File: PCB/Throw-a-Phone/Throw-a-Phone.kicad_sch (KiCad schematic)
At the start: 30 parts, among them J1 GSM Module Left, J2 GSM Module Right, J3 Conn_01x04_Pin, SW1 SW_Push, SW10 SW_Push, SW11 SW_Push, SW12 SW_Push, SW2 SW_Push, SW3 SW_Push, SW4 SW_Push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

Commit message: Made PCB, fixed design
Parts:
- J1, J2: footprint (none) -> Connector_PinHeader_2.00mm:PinHeader_1x07_P2.00mm_Vertical
- J3: footprint (none) -> footprints:SSD1306-0.91-OLED-4pin-128x32
- LS1, MK1: footprint (none) -> Connector_PinHeader_2.00mm:PinHeader_1x02_P2.00mm_Vertical
- SW1, SW10, SW11, SW12, SW2, SW3, SW4, SW5, SW6, SW7, SW8, SW9: footprint (none) -> Button_Switch_THT:SW_PUSH_6mm_H5mm
- U1: footprint ESP32-C3_SUPERMINI_TH:MODULE_ESP32-C3_SUPERMINI_TH -> footprints:MODULE_ESP32-C3_SUPERMINI_TH
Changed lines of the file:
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@@
 			)
 		)
-		(property "Footprint" "ESP32-C3_SUPERMINI_TH:MODULE_ESP32-C3_SUPERMINI_TH"
+		(property "Footprint" "footprints:MODULE_ESP32-C3_SUPERMINI_TH"
 			(at 163.83 102.87 0)
 			(effects
@@
 			)
 		)
-		(property "Footprint" ""
+		(property "Footprint" "Button_Switch_THT:SW_PUSH_6mm_H5mm"
 			(at 81.28 147.32 0)
 			(effects
@@
 			)
 		)
-		(property "Footprint" ""
+		(property "Footprint" "Button_Switch_THT:SW_PUSH_6mm_H5mm"
 			(at 55.88 71.12 0)
 			(effects
@@
 			)
 		)
-		(property "Footprint" ""
+		(property "Footprint" "Button_Switch_THT:SW_PUSH_6mm_H5mm"
 			(at 106.68 96.52 0)
 			(effects
@@
 			)
 		)
-		(property "Footprint" ""
+		(property "Footprint" "Button_Switch_THT:SW_PUSH_6mm_H5mm"
 			(at 81.28 96.52 0)
 			(effects
@@
 			)
 		)
-		(property "Footprint" ""
+		(property "Footprint" "Connector_PinHeader_2.00mm:PinHeader_1x02_P2.00mm_Vertical"
 			(at 255.27 120.65 0)
 			(effects
@@
 			)
 		)
-		(property "Footprint" ""
+		(property "Footprint" "Button_Switch_THT:SW_PUSH_6mm_H5mm"
 			(at 55.88 96.52 0)
 			(effects
@@
 			)
 		)
-		(property "Footprint" ""
+		(property "Footprint" "Button_Switch_THT:SW_PUSH_6mm_H5mm"
 			(at 55.88 147.32 0)
 			(effects
@@
 			)
 		)
-		(property "Footprint" ""
+		(property "Footprint" "Connector_PinHeader_2.00mm:PinHeader_1x02_P2.00mm_Vertical"
 			(at 226.06 118.11 90)
 			(effects
@@
 			)
 		)
-		(property "Footprint" ""
+		(property "Footprint" "Button_Switch_THT:SW_PUSH_6mm_H5mm"
 			(at 81.28 71.12 0)
 			(effects
@@
 			)
 		)
-		(property "Footprint" ""
+		(property "Footprint" "Button_Switch_THT:SW_PUSH_6mm_H5mm"
 			(at 81.28 121.92 0)
 			(effects
@@
 			)
 		)
-		(property "Footprint" ""
+		(property "Footprint" "Connector_PinHeader_2.00mm:PinHeader_1x07_P2.00mm_Vertical"
 			(at 243.84 87.63 0)
 			(effects
@@
 			)
 		)
-		(property "Footprint" ""
+		(property "Footprint" "Button_Switch_THT:SW_PUSH_6mm_H5mm"
 			(at 106.68 121.92 0)
 			(effects
@@
 			)
 		)
-		(property "Footprint" ""
+		(property "Footprint" "Button_Switch_THT:SW_PUSH_6mm_H5mm"
 			(at 106.68 71.12 0)
 			(effects
@@
 			)
 		)
-		(property "Footprint" ""
+		(property "Footprint" "Button_Switch_THT:SW_PUSH_6mm_H5mm"
 			(at 55.88 121.92 0)
 			(effects
@@
 			)
 		)
-		(property "Footprint" ""
+		(property "Footprint" "Connector_PinHeader_2.00mm:PinHeader_1x07_P2.00mm_Vertical"
 			(at 228.6 90.17 0)
 			(effects
@@
 			)
 		)
-		(property "Footprint" ""
+		(property "Footprint" "Button_Switch_THT:SW_PUSH_6mm_H5mm"
 			(at 106.68 147.32 0)
 			(effects
@@
 			)
 		)
-		(property "Footprint" ""
+		(property "Footprint" "footprints:SSD1306-0.91-OLED-4pin-128x32"
 			(at 158.75 53.34 0)
 			(effects

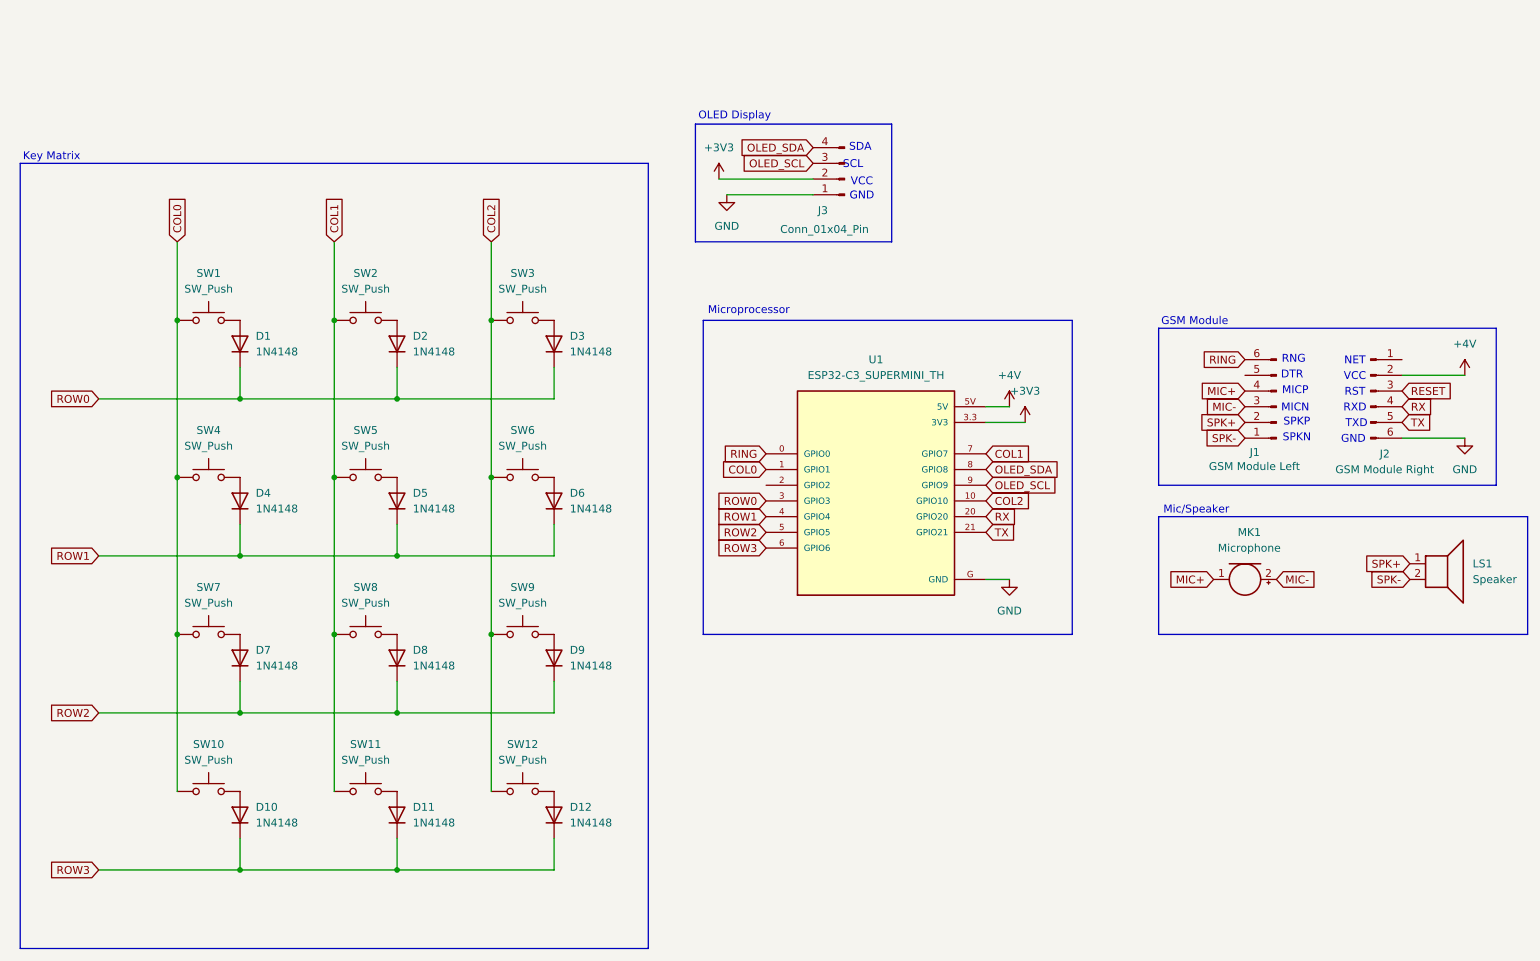
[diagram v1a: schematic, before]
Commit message: Updated readme, added images. Fixed PCB edge cuts
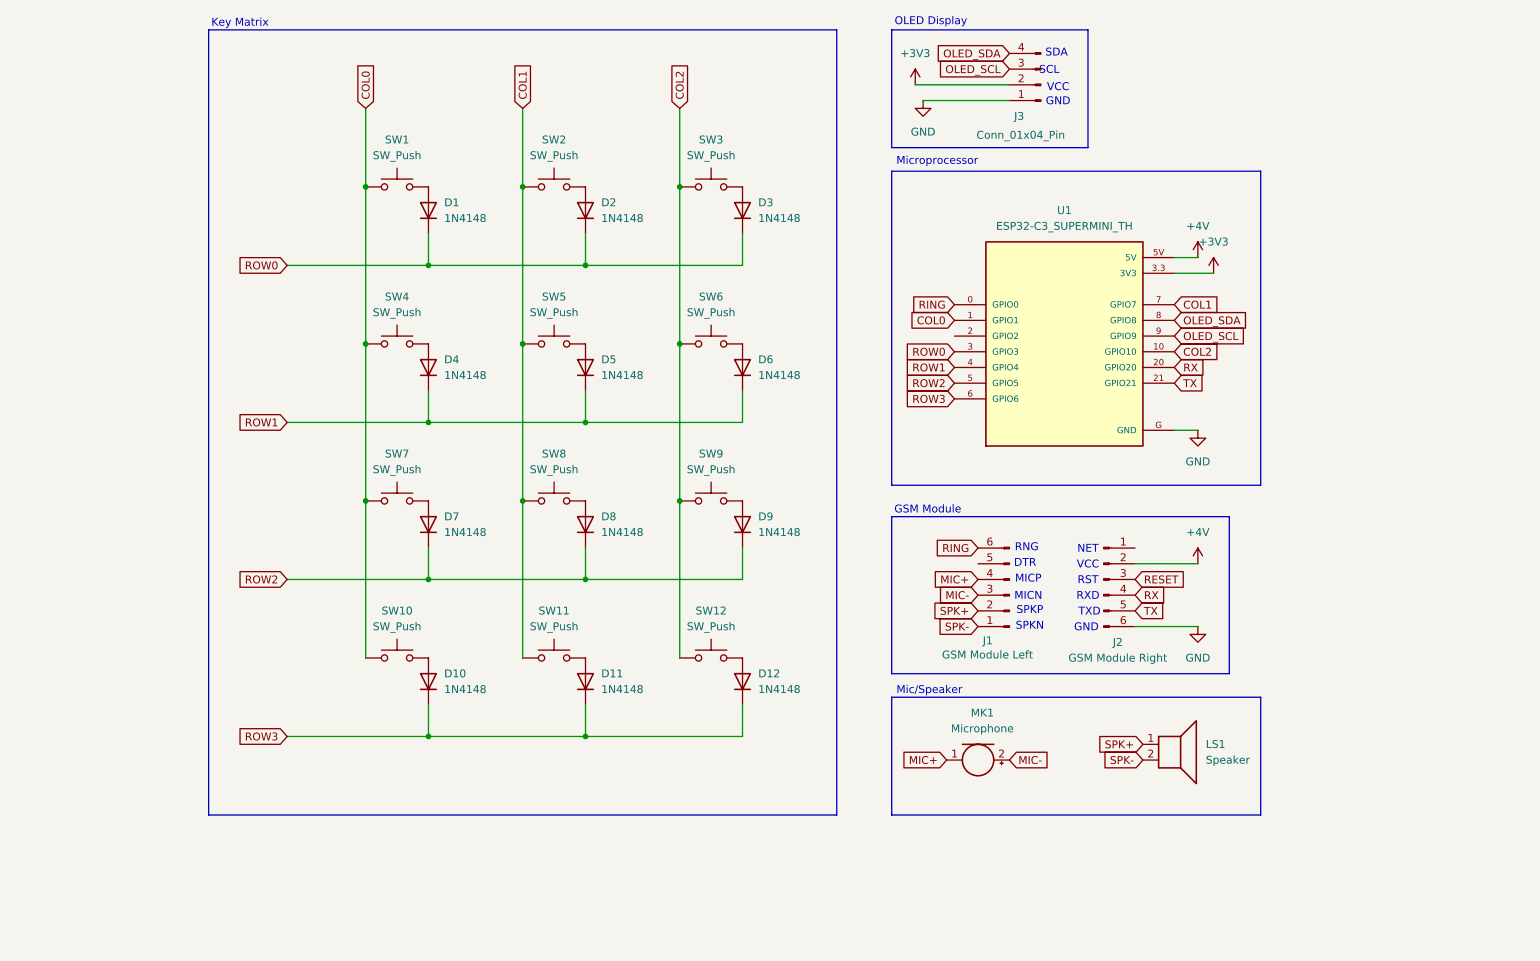
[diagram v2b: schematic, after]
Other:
- moved on the sheet: D1, D10, D11, D12, D2, D3, D4, D5, D6, D7, D8, D9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
